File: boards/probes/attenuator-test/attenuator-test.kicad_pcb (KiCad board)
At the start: 4 copper layers, 45.6 x 10 mm, 8 parts, among them J1 Conn_Coaxial, J2 Conn_Coaxial

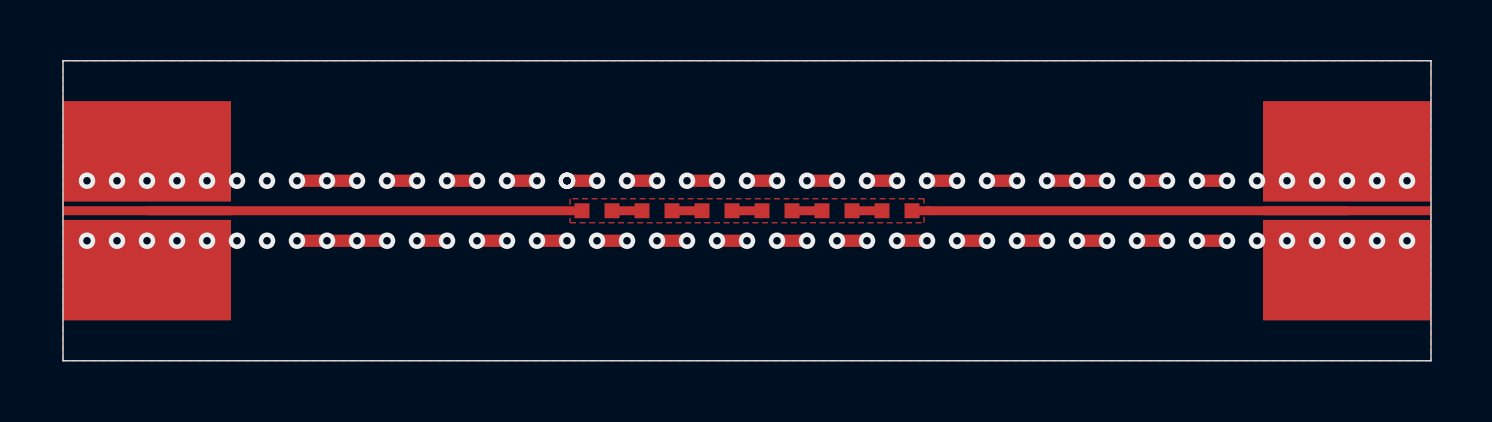
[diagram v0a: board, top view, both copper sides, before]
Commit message: Updated attenuator-test board with new, closer resistor spacing for v0.2
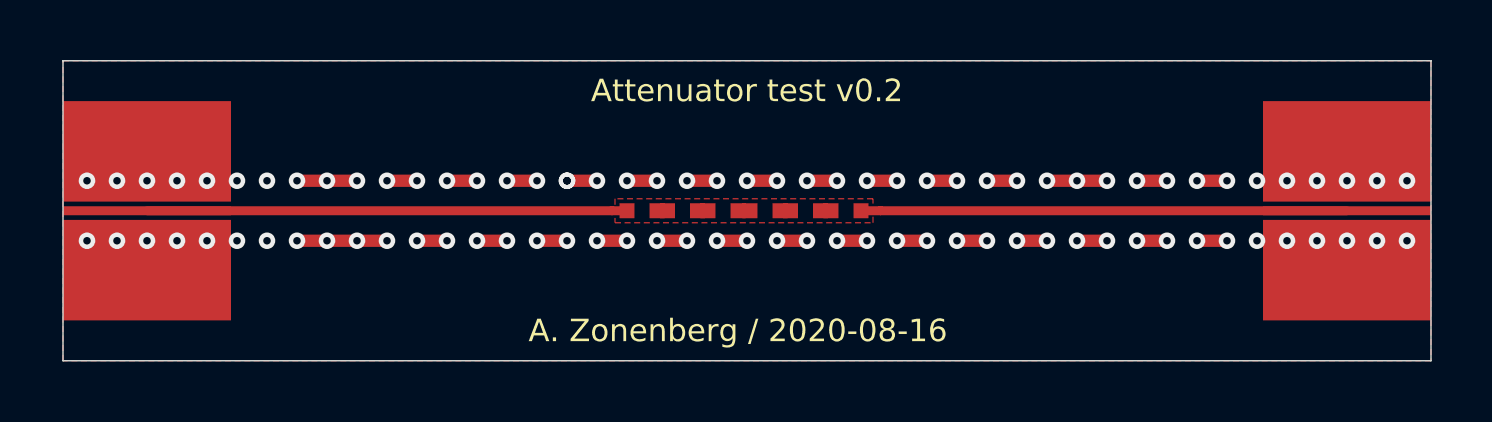
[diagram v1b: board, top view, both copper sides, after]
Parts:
- moved R6 1.70 mm to (133.3, 80.0)
- moved R1 1.50 mm to (126.5, 80.0)
- moved R5 1.05 mm to (131.9, 80.0)
- moved R2 0.85 mm to (127.8, 80.0)
- moved R4 0.40 mm to (130.6, 80.0)
- moved R3 0.20 mm to (129.2, 80.0)
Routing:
- net Net-(J2-Pad1): track 14.5 -> 16.2 mm
- net /SIGNAL: track 14.5 -> 16.0 mm
- net Net-(R4-Pad1): track 1.00 -> 0.35 mm
- net Net-(R2-Pad1): track 1.00 -> 0.35 mm
- net Net-(R1-Pad1): track 1.00 -> 0.35 mm
- net Net-(R5-Pad1): track 1.00 -> 0.35 mm
- net Net-(R3-Pad1): track 1.00 -> 0.40 mm
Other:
- board text added: "A. Zonenberg / 2020-08-16"
- board text added: "Attenuator test v0.2"
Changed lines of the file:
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@@
   (general
     (thickness 1.6)
-    (drawings 4)
-    (tracks 191)
+    (drawings 6)
+    (tracks 192)
     (zones 0)
     (modules 8)
@@
   )
   (module azonenberg_pcb:EIA_0402_RES_NOSILK_FLIPCHIP (layer F.Cu)
-    (at 135 80 180)
+    (at 133.3 80 180)
     (solder_paste_margin -0.1)
     (fp_text reference R6 (at 0 1.5) (layer F.SilkS) hide
@@
   )
   (module azonenberg_pcb:EIA_0402_RES_NOSILK_FLIPCHIP (layer F.Cu)
-    (at 133 80 180)
+    (at 131.95 80 180)
     (solder_paste_margin -0.1)
     (fp_text reference R5 (at 0 1.5) (layer F.SilkS) hide
@@
   )
   (module azonenberg_pcb:EIA_0402_RES_NOSILK_FLIPCHIP (layer F.Cu)
-    (at 131 80 180)
+    (at 130.6 80 180)
     (solder_paste_margin -0.1)
     (fp_text reference R4 (at 0 1.5) (layer F.SilkS) hide
@@
   )
   (module azonenberg_pcb:EIA_0402_RES_NOSILK_FLIPCHIP (layer F.Cu)
-    (at 129 80 180)
+    (at 129.2 80 180)
     (solder_paste_margin -0.1)
     (fp_text reference R3 (at 0 1.5) (layer F.SilkS) hide
@@
   )
   (module azonenberg_pcb:EIA_0402_RES_NOSILK_FLIPCHIP (layer F.Cu)
-    (at 127 80 180)
+    (at 127.85 80 180)
     (solder_paste_margin -0.1)
     (fp_text reference R2 (at 0 1.5) (layer F.SilkS) hide
@@
   )
   (module azonenberg_pcb:EIA_0402_RES_NOSILK_FLIPCHIP (layer F.Cu)
-    (at 125 80 180)
+    (at 126.5 80 180)
     (solder_paste_margin -0.1)
     (fp_text reference R1 (at 0 1.5) (layer F.SilkS) hide
@@
       (rotate (xyz 90 0 0))
     )
+  )
+  (gr_text "A. Zonenberg / 2020-08-16" (at 129.7 84) (layer F.SilkS)
+    (effects (font (size 0.75 0.75) (thickness 0.1)))
+  )
+  (gr_text "Attenuator test v0.2" (at 130 76) (layer F.SilkS)
+    (effects (font (size 0.75 0.75) (thickness 0.1)))
   )
   (gr_line (start 152.8 75) (end 107.2 75) (layer Edge.Cuts) (width 0.05))
@@
   (via (at 152 81) (size 0.55) (drill 0.25) (layers F.Cu B.Cu) (net 1))
   (segment (start 151 81) (end 152 81) (width 0.3) (layer F.Cu) (net 1))
-  (segment (start 110 80) (end 124.5 80) (width 0.3) (layer F.Cu) (net 2))
-  (segment (start 136.05 80) (end 150 80) (width 0.3) (layer F.Cu) (net 3))
-  (segment (start 135.5 80) (end 136.05 80) (width 0.3) (layer F.Cu) (net 3))
-  (segment (start 125.5 80) (end 126.5 80) (width 0.3) (layer F.Cu) (net 4))
-  (segment (start 127.5 80) (end 128.5 80) (width 0.3) (layer F.Cu) (net 5))
-  (segment (start 129.5 80) (end 130.5 80) (width 0.3) (layer F.Cu) (net 6))
-  (segment (start 131.5 80) (end 132.5 80) (width 0.3) (layer F.Cu) (net 7))
-  (segment (start 133.5 80) (end 134.5 80) (width 0.3) (layer F.Cu) (net 8))
+  (segment (start 125.5 80) (end 126 80) (width 0.3) (layer F.Cu) (net 2))
+  (segment (start 110 80) (end 125.5 80) (width 0.3) (layer F.Cu) (net 2))
+  (segment (start 134.45 80) (end 133.8 80) (width 0.3) (layer F.Cu) (net 3))
+  (segment (start 150 80) (end 134.45 80) (width 0.3) (layer F.Cu) (net 3))
+  (segment (start 127 80) (end 127.35 80) (width 0.3) (layer F.Cu) (net 4))
+  (segment (start 128.35 80) (end 128.7 80) (width 0.3) (layer F.Cu) (net 5))
+  (segment (start 129.7 80) (end 130.1 80) (width 0.3) (layer F.Cu) (net 6))
+  (segment (start 131.1 80) (end 131.45 80) (width 0.3) (layer F.Cu) (net 7))
+  (segment (start 132.45 80) (end 132.8 80) (width 0.3) (layer F.Cu) (net 8))
   (zone (net 1) (net_name /GND) (layer In1.Cu) (hatch edge 0.508)
     (connect_pads yes (clearance 0.2))
@@
     (polygon
       (pts
-        (xy 124.1 79.6) (xy 124.1 80.4) (xy 135.9 80.4) (xy 135.9 79.6)
+        (xy 125.6 79.6) (xy 125.6 80.4) (xy 134.2 80.4) (xy 134.2 79.6)
       )
     )
@@
     (polygon
       (pts
-        (xy 125.9 79.5) (xy 125.9 80.5) (xy 126.1 80.5) (xy 126.1 79.5)
+        (xy 125.3 79.5) (xy 125.3 80.5) (xy 125.5 80.5) (xy 125.5 79.5)
       )
     )
     (polygon
       (pts
-        (xy 127.9 79.5) (xy 127.9 80.5) (xy 128.1 80.5) (xy 128.1 79.5)
+        (xy 134.3 79.5) (xy 134.3 80.5) (xy 134.5 80.5) (xy 134.5 79.5)
       )
     )
-    (polygon
-      (pts
-        (xy 129.9 79.5) (xy 129.9 80.5) (xy 130.1 80.5) (xy 130.1 79.5)
-      )
-    )
-    (polygon
-      (pts
-        (xy 123.8 79.5) (xy 123.8 80.5) (xy 124 80.5) (xy 124 79.5)
-      )
-    )
-    (polygon
-      (pts
-        (xy 131.9 79.5) (xy 131.9 80.5) (xy 132.1 80.5) (xy 132.1 79.5)
-      )
-    )
-    (polygon
-      (pts
-        (xy 133.9 79.5) (xy 133.9 80.5) (xy 134.1 80.5) (xy 134.1 79.5)
-      )
-    )
-    (polygon
-      (pts
-        (xy 136 79.5) (xy 136 80.5) (xy 136.2 80.5) (xy 136.2 79.5)
-      )
-    )

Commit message: New closer spaced variant
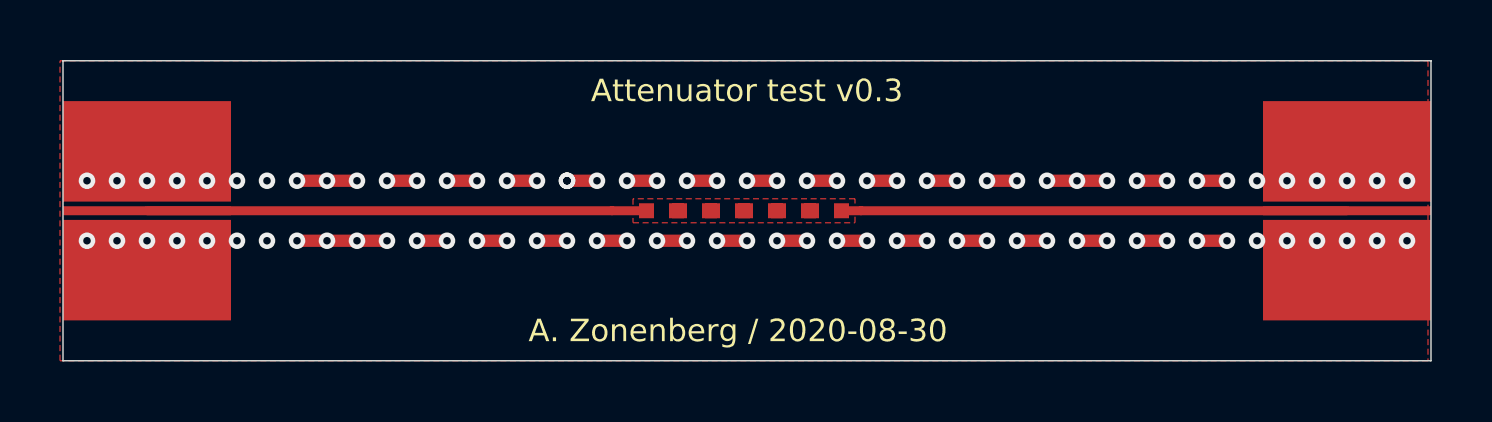
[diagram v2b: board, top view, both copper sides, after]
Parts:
- moved R1 0.65 mm to (127.2, 80.0)
- moved R6 0.65 mm to (132.7, 80.0)
- moved R2 0.40 mm to (128.2, 80.0)
- moved R5 0.40 mm to (131.6, 80.0)
- moved R3 0.15 mm to (129.3, 80.0)
- moved R4 0.15 mm to (130.4, 80.0)
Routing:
- net Net-(J2-Pad1): track 16.2 -> 16.8 mm
- net /SIGNAL: track 16.0 -> 16.6 mm
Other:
- board text added: "A. Zonenberg / 2020-08-30"
- board text added: "Attenuator test v0.3"
- board text removed: "A. Zonenberg / 2020-08-16"
- board text removed: "Attenuator test v0.2"
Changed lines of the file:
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@@
     (thickness 1.6)
     (drawings 6)
-    (tracks 192)
+    (tracks 187)
     (zones 0)
     (modules 8)
@@
     (visible_elements FFFFFF7F)
     (pcbplotparams
-      (layerselection 0x010c8_ffffffff)
+      (layerselection 0x010e8_ffffffff)
       (usegerberextensions false)
       (usegerberattributes false)
@@
   )
   (module azonenberg_pcb:EIA_0402_RES_NOSILK_FLIPCHIP (layer F.Cu)
-    (at 133.3 80 180)
-    (solder_paste_margin -0.1)
+    (at 132.65 80 180)
+    (solder_paste_margin -0.06)
     (fp_text reference R6 (at 0 1.5) (layer F.SilkS) hide
       (effects (font (size 1 1) (thickness 0.15)))
@@
   )
   (module azonenberg_pcb:EIA_0402_RES_NOSILK_FLIPCHIP (layer F.Cu)
-    (at 131.95 80 180)
-    (solder_paste_margin -0.1)
+    (at 131.55 80 180)
+    (solder_paste_margin -0.06)
     (fp_text reference R5 (at 0 1.5) (layer F.SilkS) hide
       (effects (font (size 1 1) (thickness 0.15)))
@@
   )
   (module azonenberg_pcb:EIA_0402_RES_NOSILK_FLIPCHIP (layer F.Cu)
-    (at 130.6 80 180)
-    (solder_paste_margin -0.1)
+    (at 130.45 80 180)
+    (solder_paste_margin -0.06)
     (fp_text reference R4 (at 0 1.5) (layer F.SilkS) hide
       (effects (font (size 1 1) (thickness 0.15)))
@@
   )
   (module azonenberg_pcb:EIA_0402_RES_NOSILK_FLIPCHIP (layer F.Cu)
-    (at 129.2 80 180)
-    (solder_paste_margin -0.1)
+    (at 129.35 80 180)
+    (solder_paste_margin -0.06)
     (fp_text reference R3 (at 0 1.5) (layer F.SilkS) hide
       (effects (font (size 1 1) (thickness 0.15)))
@@
   )
   (module azonenberg_pcb:EIA_0402_RES_NOSILK_FLIPCHIP (layer F.Cu)
-    (at 127.85 80 180)
-    (solder_paste_margin -0.1)
+    (at 128.25 80 180)
+    (solder_paste_margin -0.06)
     (fp_text reference R2 (at 0 1.5) (layer F.SilkS) hide
       (effects (font (size 1 1) (thickness 0.15)))
@@
   )
   (module azonenberg_pcb:EIA_0402_RES_NOSILK_FLIPCHIP (layer F.Cu)
-    (at 126.5 80 180)
-    (solder_paste_margin -0.1)
+    (at 127.15 80 180)
+    (solder_paste_margin -0.06)
     (fp_text reference R1 (at 0 1.5) (layer F.SilkS) hide
       (effects (font (size 1 1) (thickness 0.15)))
@@
     )
   )
-  (gr_text "A. Zonenberg / 2020-08-16" (at 129.7 84) (layer F.SilkS)
+  (gr_text "A. Zonenberg / 2020-08-30" (at 129.7 84) (layer F.SilkS)
     (effects (font (size 0.75 0.75) (thickness 0.1)))
   )
-  (gr_text "Attenuator test v0.2" (at 130 76) (layer F.SilkS)
+  (gr_text "Attenuator test v0.3" (at 130 76) (layer F.SilkS)
     (effects (font (size 0.75 0.75) (thickness 0.1)))
   )
@@
   (via (at 152 81) (size 0.55) (drill 0.25) (layers F.Cu B.Cu) (net 1))
   (segment (start 151 81) (end 152 81) (width 0.3) (layer F.Cu) (net 1))
-  (segment (start 125.5 80) (end 126 80) (width 0.3) (layer F.Cu) (net 2))
-  (segment (start 110 80) (end 125.5 80) (width 0.3) (layer F.Cu) (net 2))
-  (segment (start 134.45 80) (end 133.8 80) (width 0.3) (layer F.Cu) (net 3))
-  (segment (start 150 80) (end 134.45 80) (width 0.3) (layer F.Cu) (net 3))
-  (segment (start 127 80) (end 127.35 80) (width 0.3) (layer F.Cu) (net 4))
-  (segment (start 128.35 80) (end 128.7 80) (width 0.3) (layer F.Cu) (net 5))
-  (segment (start 129.7 80) (end 130.1 80) (width 0.3) (layer F.Cu) (net 6))
-  (segment (start 131.1 80) (end 131.45 80) (width 0.3) (layer F.Cu) (net 7))
-  (segment (start 132.45 80) (end 132.8 80) (width 0.3) (layer F.Cu) (net 8))
+  (segment (start 125.5 80) (end 110 80) (width 0.3) (layer F.Cu) (net 2))
+  (segment (start 126.625 80) (end 125.5 80) (width 0.3) (layer F.Cu) (net 2))
+  (segment (start 133.8 80) (end 133.175 80) (width 0.3) (layer F.Cu) (net 3))
+  (segment (start 150 80) (end 133.8 80) (width 0.3) (layer F.Cu) (net 3))
   (zone (net 1) (net_name /GND) (layer In1.Cu) (hatch edge 0.508)
     (connect_pads yes (clearance 0.2))
@@
     (polygon
       (pts
-        (xy 152.8 85) (xy 107.2 85) (xy 107.2 75) (xy 152.8 75)
+        (xy 152.7 85) (xy 107.1 85) (xy 107.1 75) (xy 152.7 75)
       )
     )
     (polygon
       (pts
-        (xy 125.6 79.6) (xy 125.6 80.4) (xy 134.2 80.4) (xy 134.2 79.6)
+        (xy 126.2 79.6) (xy 126.2 80.4) (xy 133.6 80.4) (xy 133.6 79.6)
       )
     )
@@
     (polygon
       (pts
-        (xy 125.3 79.5) (xy 125.3 80.5) (xy 125.5 80.5) (xy 125.5 79.5)
+        (xy 125.9 79.5) (xy 125.9 80.5) (xy 126.1 80.5) (xy 126.1 79.5)
       )
     )
     (polygon
       (pts
-        (xy 134.3 79.5) (xy 134.3 80.5) (xy 134.5 80.5) (xy 134.5 79.5)
+        (xy 133.7 79.5) (xy 133.7 80.5) (xy 133.9 80.5) (xy 133.9 79.5)
       )
     )

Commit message: New attenuator test rev with 5 resistors
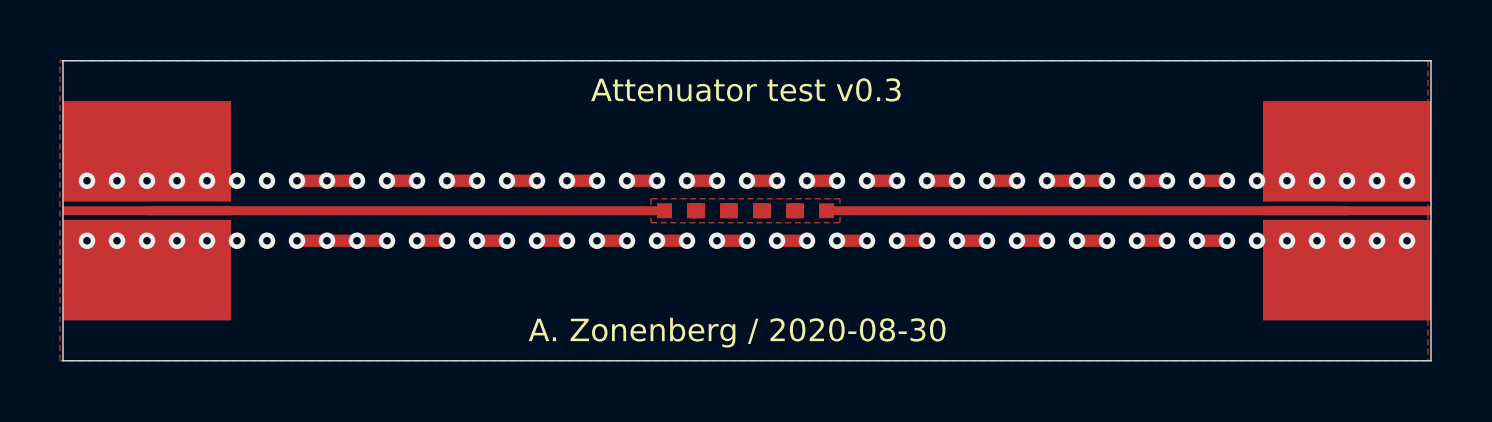
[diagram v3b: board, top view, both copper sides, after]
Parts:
- removed R1: 50, azonenberg_pcb:EIA_0402_RES_NOSILK_FLIPCHIP
- R2: value 75 -> 50
- R3, R4, R5: value 75 -> 100
- moved R2 0.50 mm to (127.8, 80.0)
- moved R3 0.50 mm to (128.8, 80.0)
- moved R4 0.50 mm to (129.9, 80.0)
- moved R5 0.50 mm to (131.1, 80.0)
- moved R6 0.50 mm to (132.2, 80.0)
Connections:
- R2 pad 2: Net-(R1-Pad1) -> /SIGNAL
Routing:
- net /SIGNAL: track 16.6 -> 17.2 mm
- net Net-(J2-Pad1): track 16.8 -> 17.3 mm
- net /GND: vias 91 -> 90
